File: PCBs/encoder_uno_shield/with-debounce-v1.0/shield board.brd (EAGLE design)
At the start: 66.4 x 53.1 mm, 33 parts, among them U1 ARDUINOR3-BPLACE

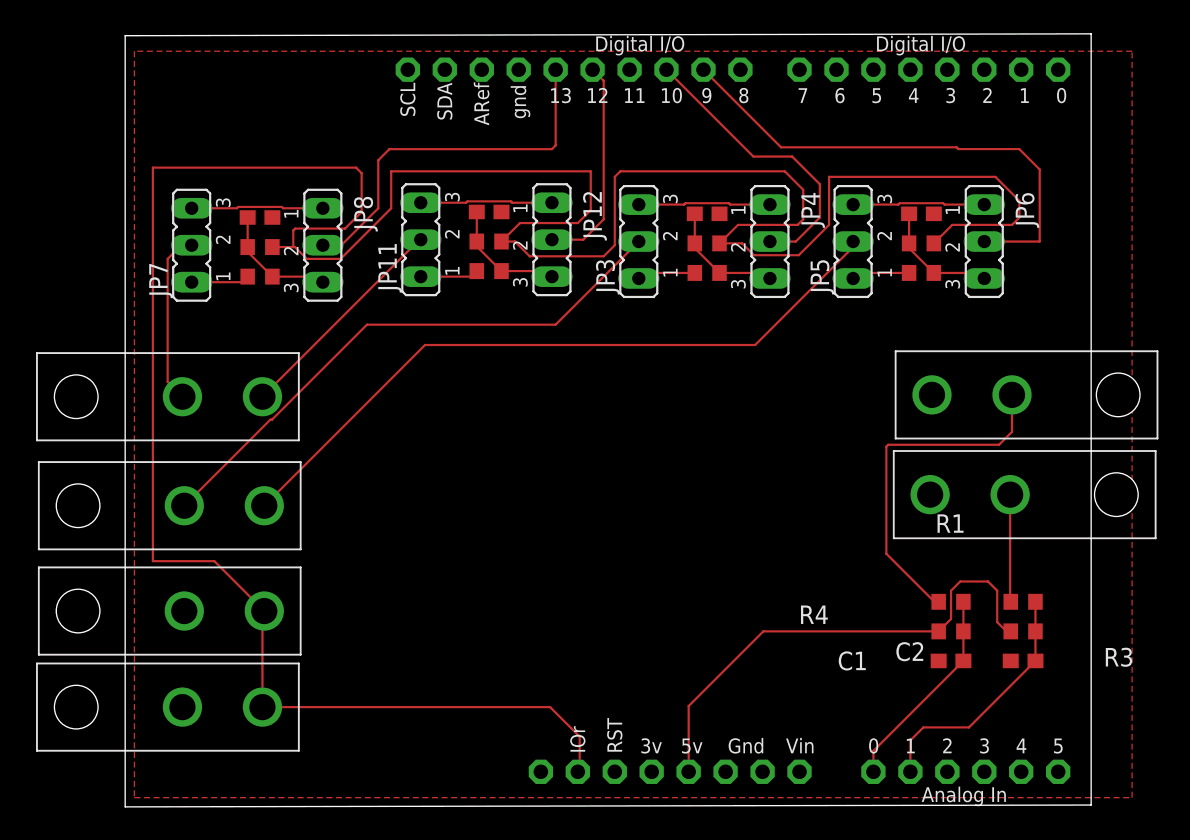
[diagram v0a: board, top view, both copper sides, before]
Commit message: realized i only need one switch port, about to redesign
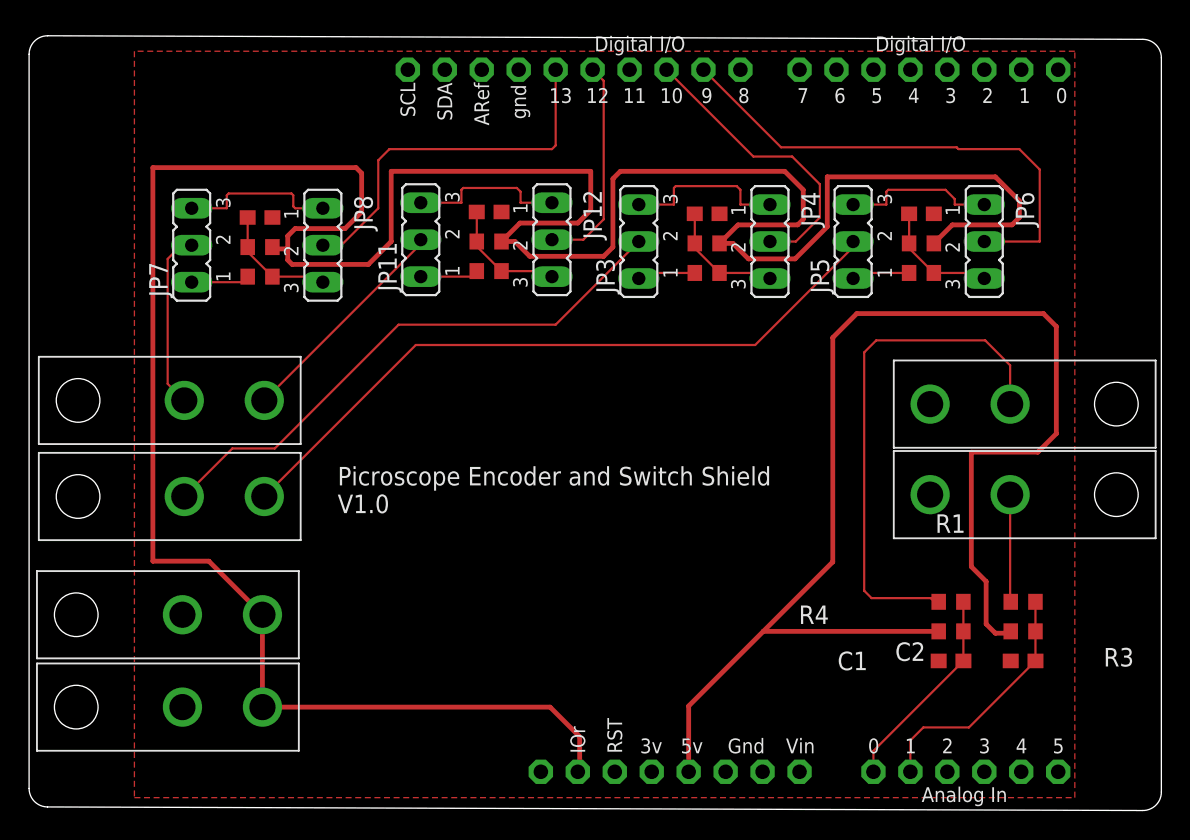
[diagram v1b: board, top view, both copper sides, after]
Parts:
- moved U$2 0.65 mm to (60.2, 27.8)
- moved U$6 0.64 mm to (3.43, 21.5)
- moved U$5 0.28 mm to (3.43, 28.1)
- moved U$4 0.28 mm to (3.30, 13.3)
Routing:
- net VCC: track 231.4 -> 289.9 mm
- net N$4: track 24.5 -> 35.6 mm
- net E2CHB_BYPASS: track 9.09 -> 11.3 mm
- net E1CHB_BYPASS: track 9.09 -> 10.8 mm
- net E1CHA_BYPASS: track 9.09 -> 10.8 mm
- net E2CHA_BYPASS: track 9.09 -> 10.6 mm
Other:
- board size 66.4 x 53.1 mm -> 77.8 x 53.3 mm
- board text added: "Picroscope Encoder and Switch Shield V1.0"
